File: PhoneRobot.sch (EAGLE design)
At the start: 52 parts, among them IC1 LP2985M5, K1 TX2-5V, K2 TX2-5V, K3 TX2-5V, K4 TX2-5V, K5 TX2-5V, Q1 2N3904SOT23, Q2 2N3904SOT23, Q3 2N3904SOT23, Q4 2N3904SOT23, Q5 2N3904SOT23, U1 G2XX3---PW20

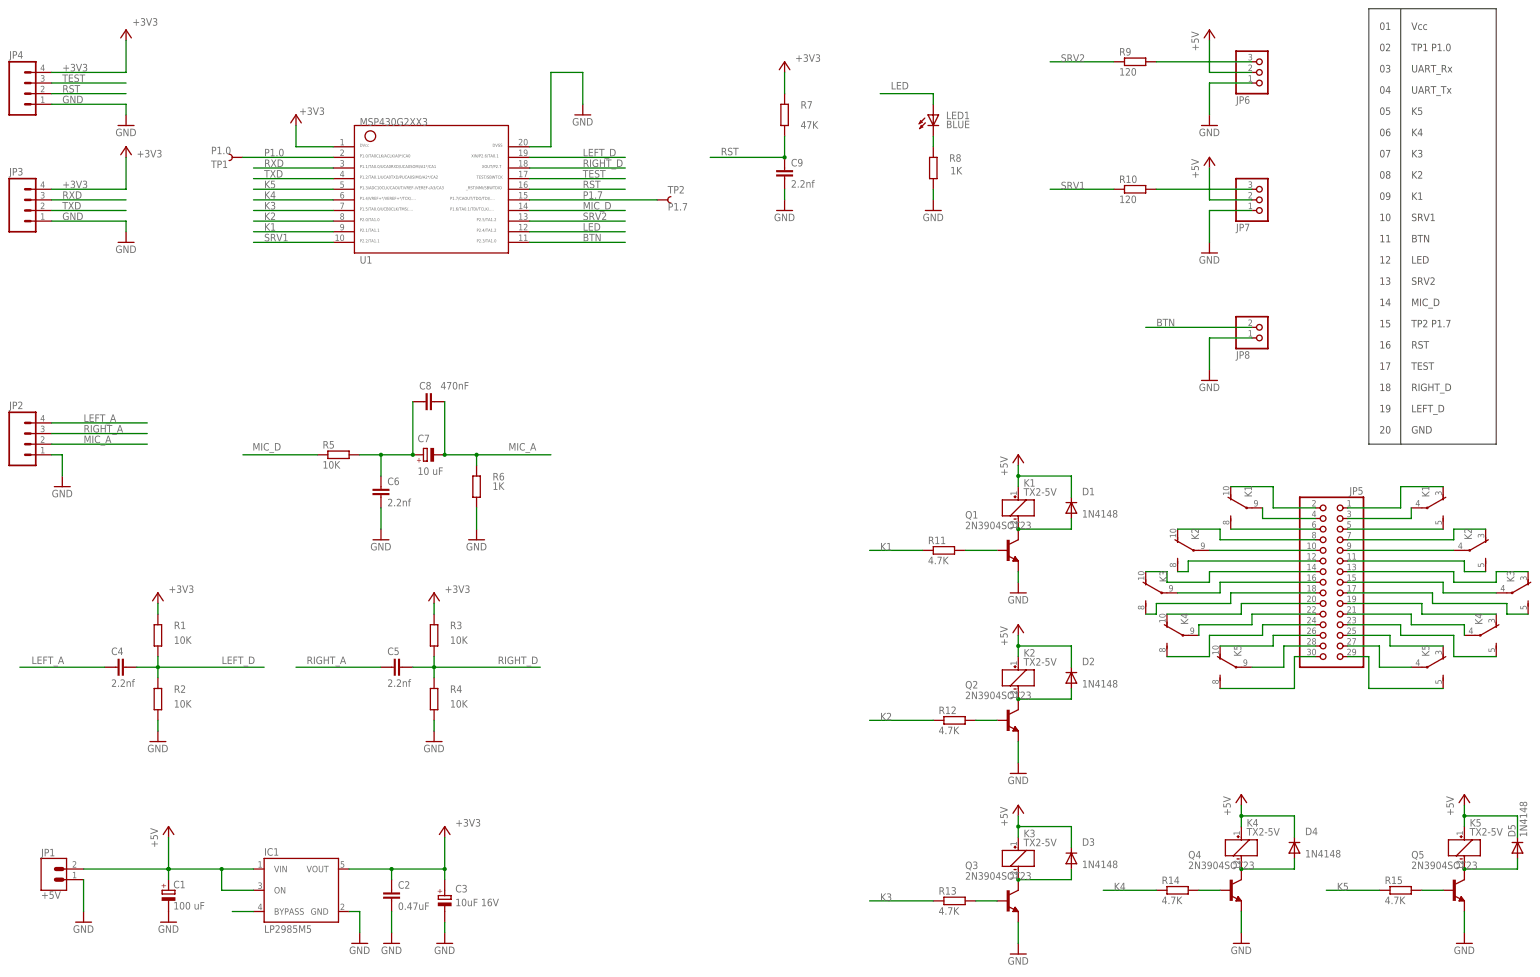
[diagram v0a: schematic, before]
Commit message: Nominals changed after soldering first version
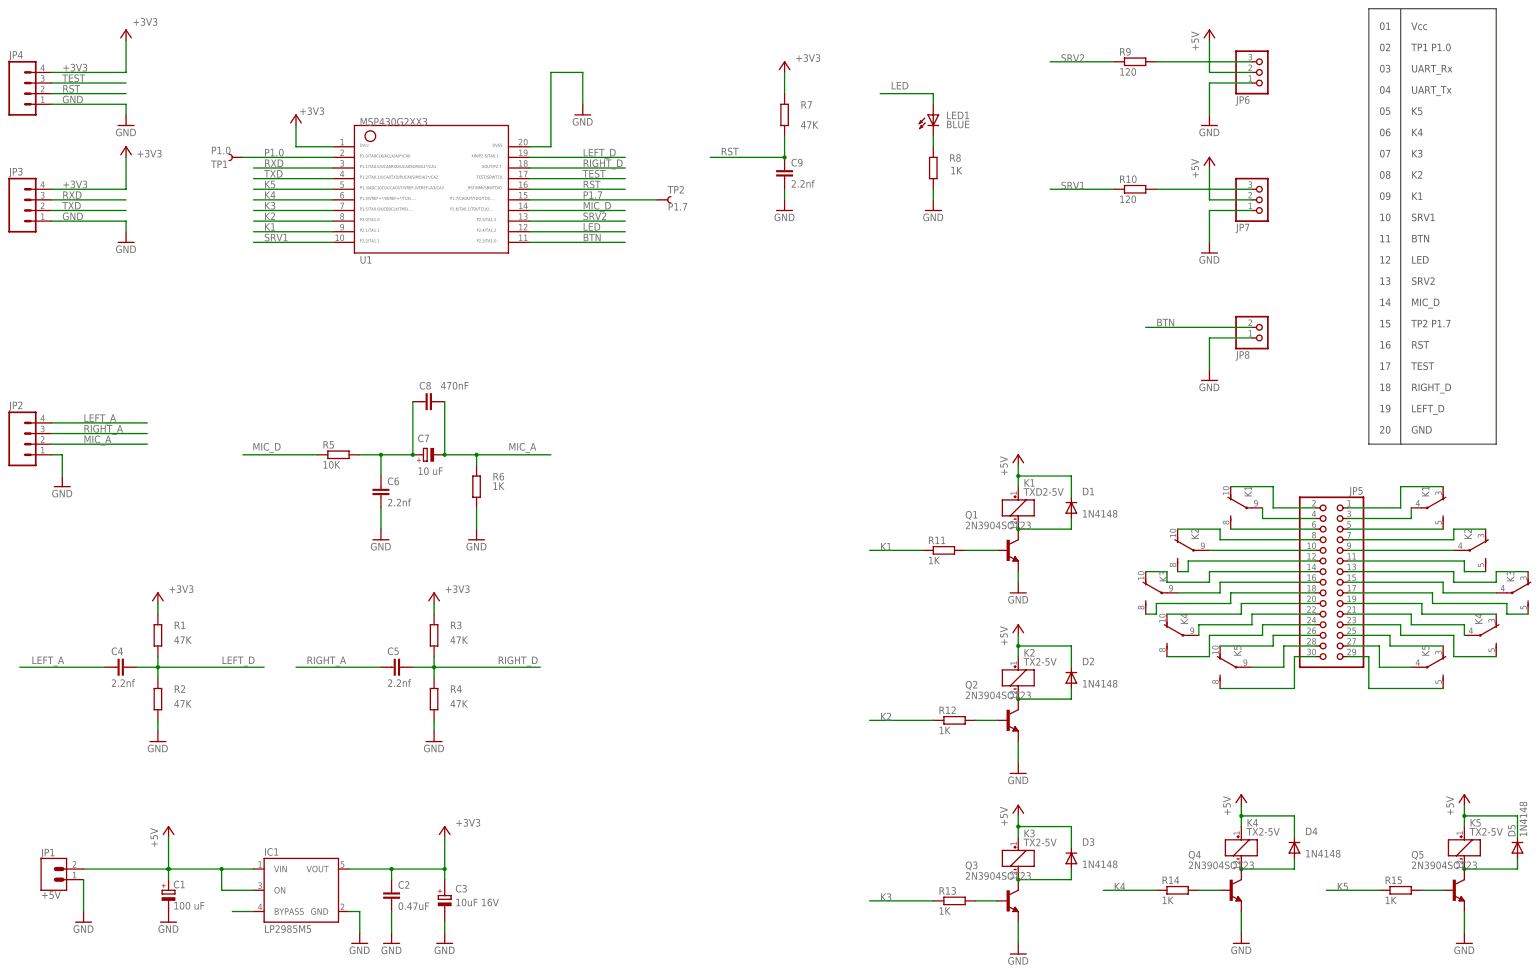
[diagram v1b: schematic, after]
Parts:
- K1: value TX2-5V -> TXD2-5V; device relay:TX2-5V -> relay:TXD2-5V
- R1, R2, R3, R4: value 10K -> 47K
- R11, R12, R13, R14, R15: value 4.7K -> 1K
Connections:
- net N$2: now also K1G$2.O; no longer K12.O
- net N$3: now also K1G$2.P; no longer K12.P
- net N$4: now also K1G$2.S; no longer K12.S
- net N$5: now also K1G$1.P; no longer K11.P
- net N$7: now also K1G$1.O; no longer K11.O
- net N$8: now also K1G$1.S; no longer K11.S

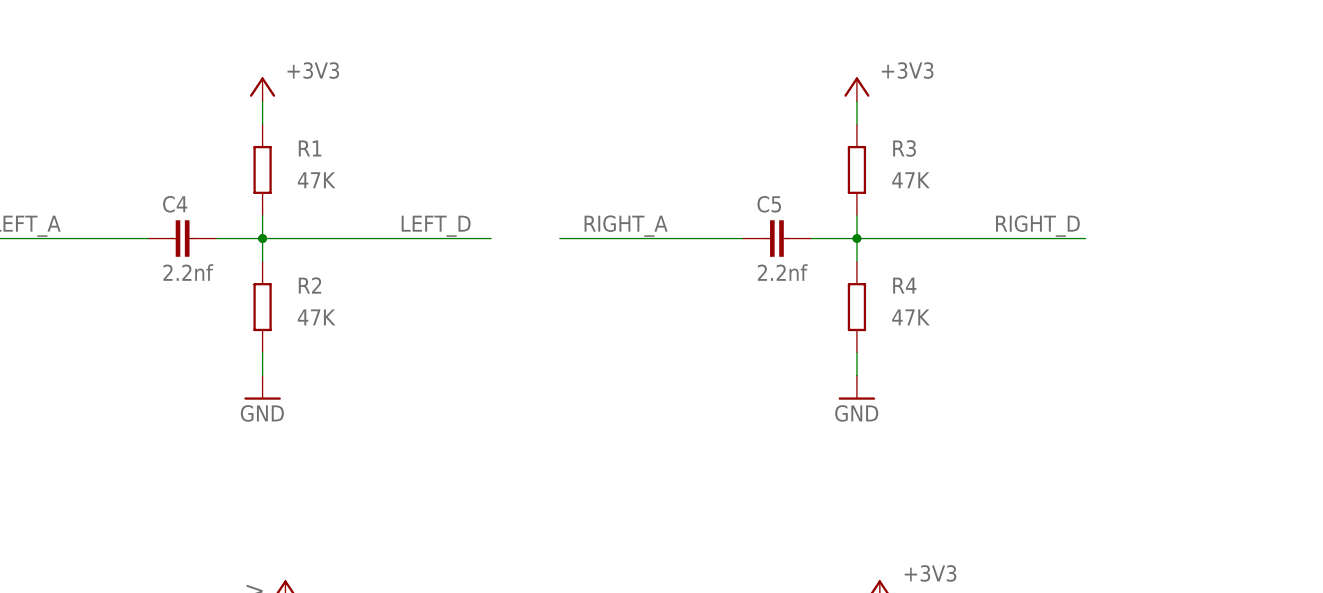
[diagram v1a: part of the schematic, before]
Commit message: Fix Audio Input schematics
Schematics only, needs to fix layout
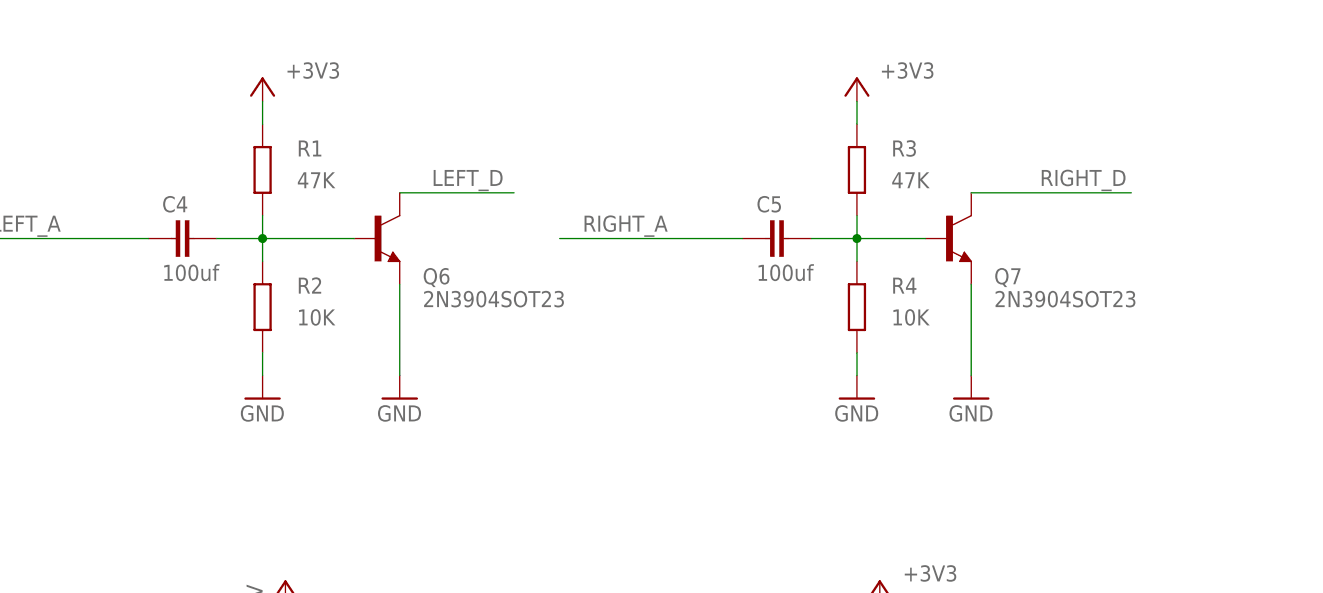
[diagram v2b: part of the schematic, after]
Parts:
- added Q6, Q7: 2N3904SOT23, transistor-npn:2N3904SOT23
- C4, C5: value 2.2nf -> 100uf
- R2, R4: value 47K -> 10K
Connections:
- new net N$12: C4.2, Q6.B, R1.1, R2.2
- new net N$46: C5.2, Q7.B, R3.1, R4.2
- net GND: now also Q6.E, Q7.E
- net LEFT_D: now also Q6.C; no longer C4.2, R1.1, R2.2
- net RIGHT_D: now also Q7.C; no longer C5.2, R3.1, R4.2
